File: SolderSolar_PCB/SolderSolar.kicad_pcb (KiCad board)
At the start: 2 copper layers, 50 x 37.5 mm, 14 parts, among them P1 SOLAR_V, P2 LOGO1, P3 LOGO2, P4 PCB, P5 LOGO3, SW1 RED, SW2 WHITE

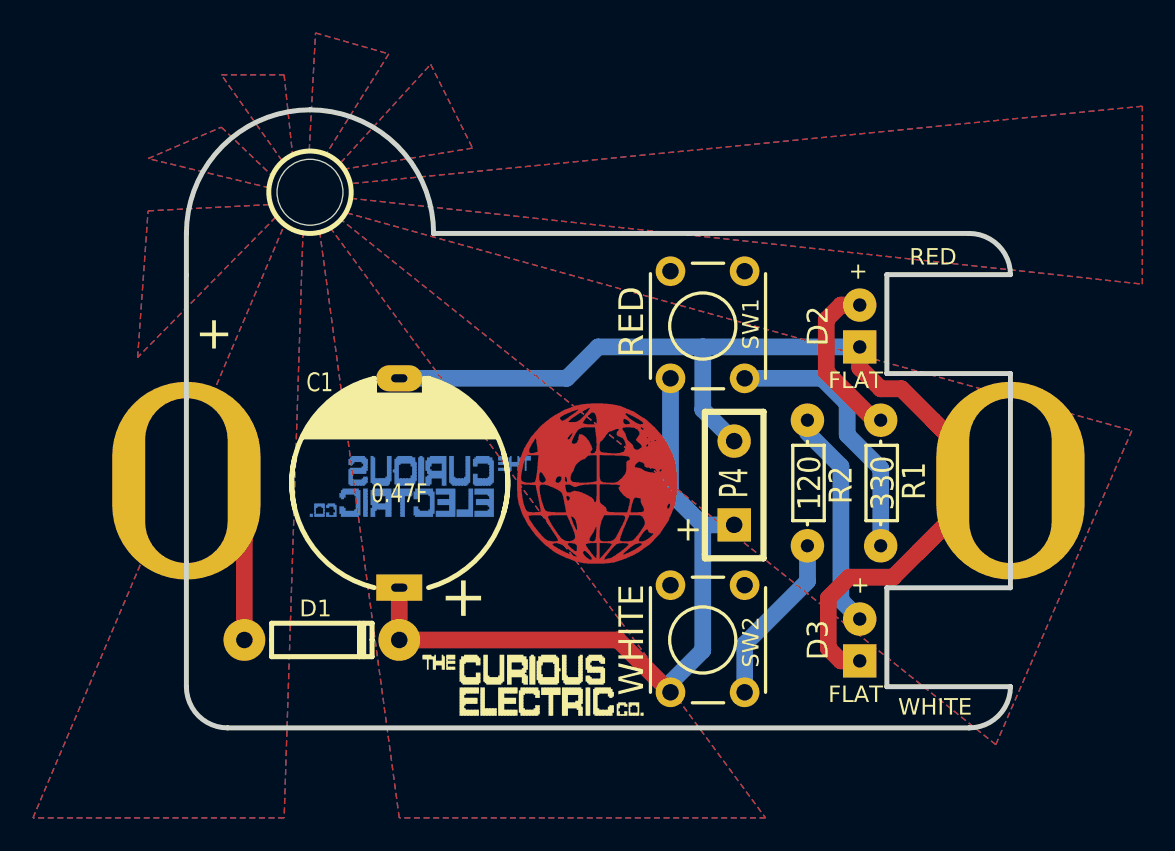
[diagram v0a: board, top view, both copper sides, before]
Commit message: Updated PCB for KiCAD
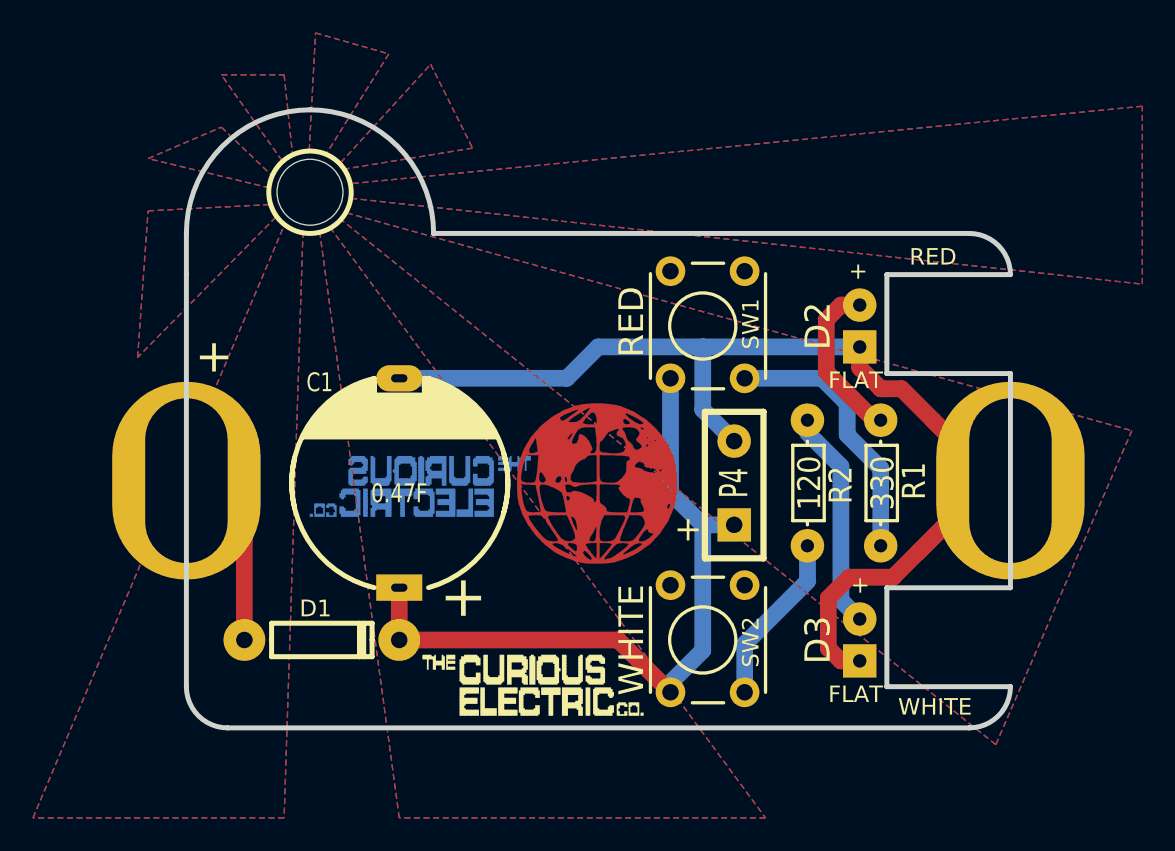
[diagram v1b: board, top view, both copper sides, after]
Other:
- rule pad_to_mask_clearance: 0.2 -> 0

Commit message: updated to kicad 6. updated PCB
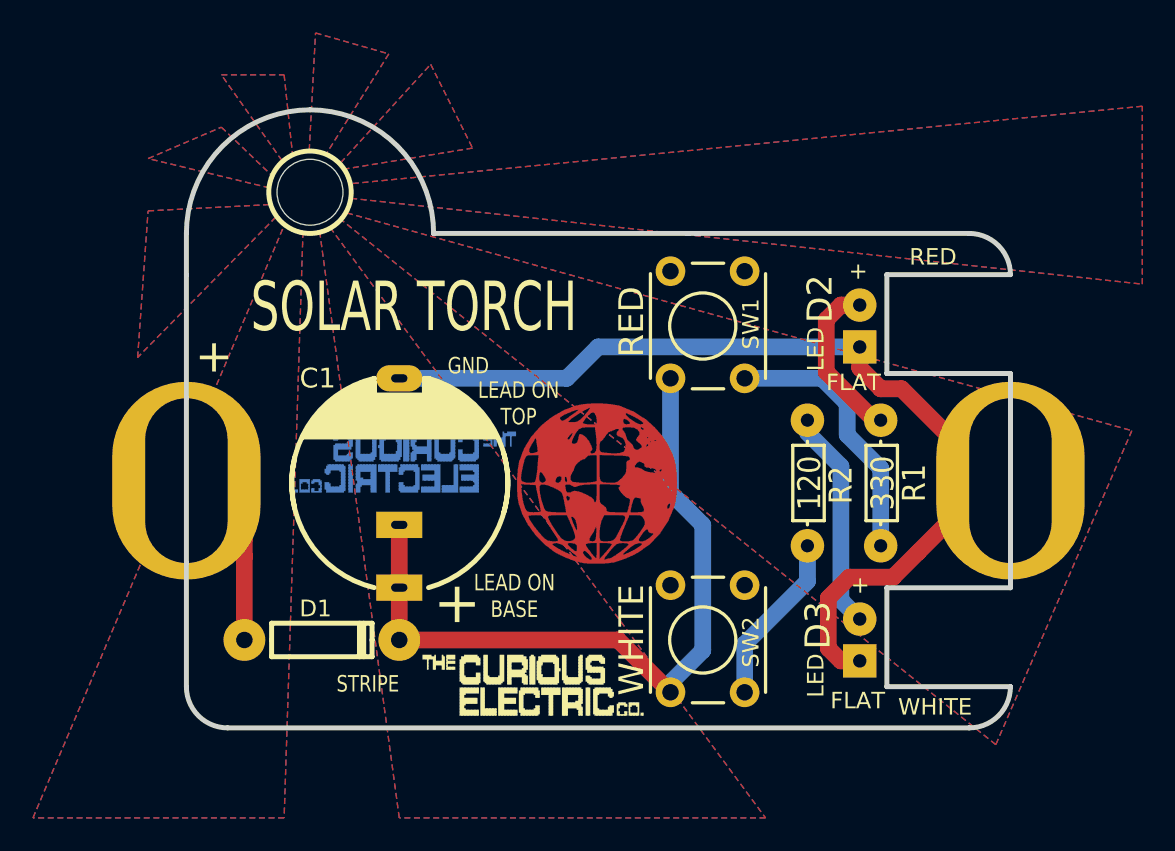
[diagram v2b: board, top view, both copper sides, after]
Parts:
- removed P4: PCB, matts_components:SIL-2_wide_lg_pad
- C1: footprint REInnovationFootprint:C_0_47F_SuperCap -> REInnovationFootprint:C_0_47F_SuperCap_2POS
- moved P5 1.73 mm to (124.8, 55.0)
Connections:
- P2 pad 1: (no net) -> unconnected-(P2-Pad1)
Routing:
- net GND: track 79.3 -> 63.4 mm
- net Net-(D1-Pad2): track 13.6 -> 19.5 mm
- net Net-(C1-Pad1): track 43.7 -> 45.6 mm
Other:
- net class Default removed
- board text added: "BIG BLOB OF SOLDER!"
- board text added: "BIG BLOB SOLDER!"
- board text added: "GND"
- board text added: "LEAD ON BASE"
- board text added: "LEAD ON TOP"
- board text added: "LED"
- board text added: "SOLAR PANEL FITS ON THIS SIDE"
- board text added: "SOLAR TORCH"
- board text added: "STRIPE"
- board text removed: "+"
